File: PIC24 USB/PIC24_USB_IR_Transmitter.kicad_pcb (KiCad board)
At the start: 2 copper layers, 38 parts, among them CON1 USB-MINI-B, P1 CONN_6, P2 CONN_4, P3 CONN_6, P4 CONN_6, P5 CONN_4, P6 CONN_1, P7 CONN_8, P8 CONN_8X2, Q1 2N7002, U1 PIC24FJXXXGB106, U2 LM1117_SOT223_3V3, X1 CRYSTAL_12MHZ

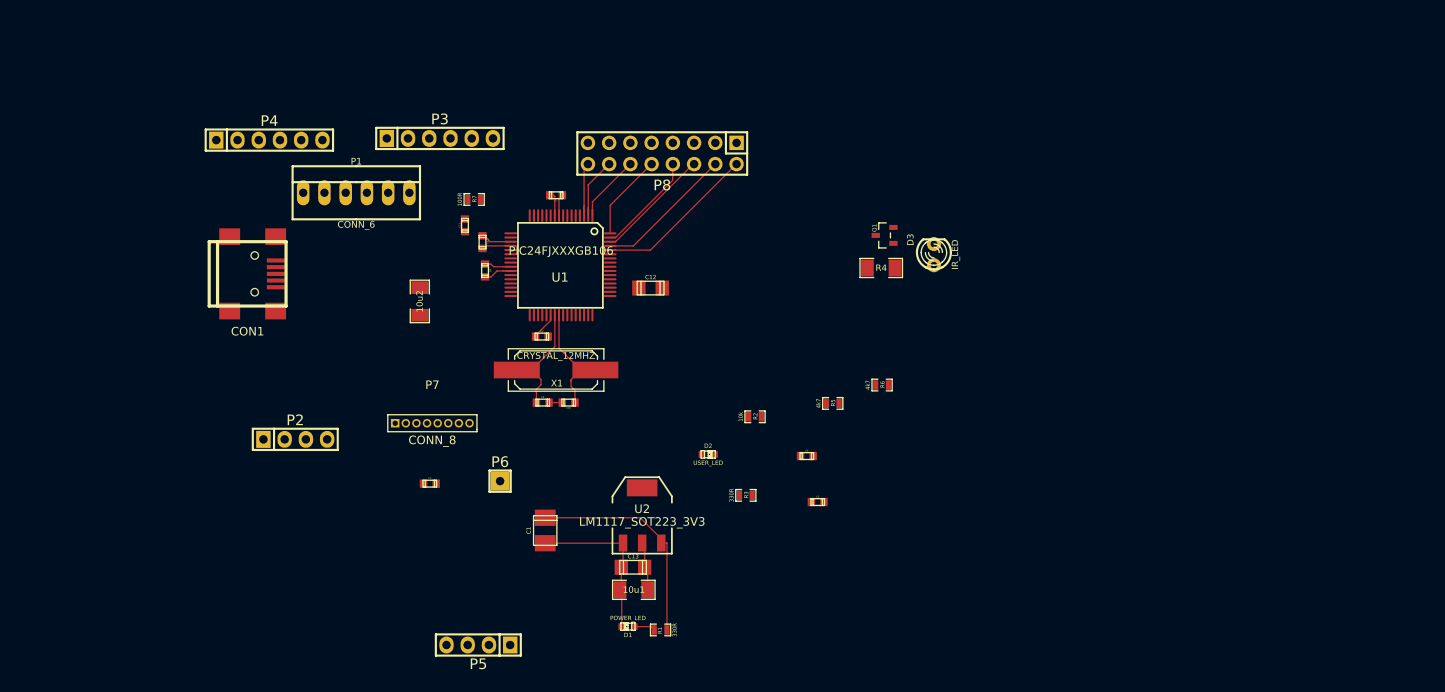
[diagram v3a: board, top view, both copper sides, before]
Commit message: added led display, many additional headers and DAC
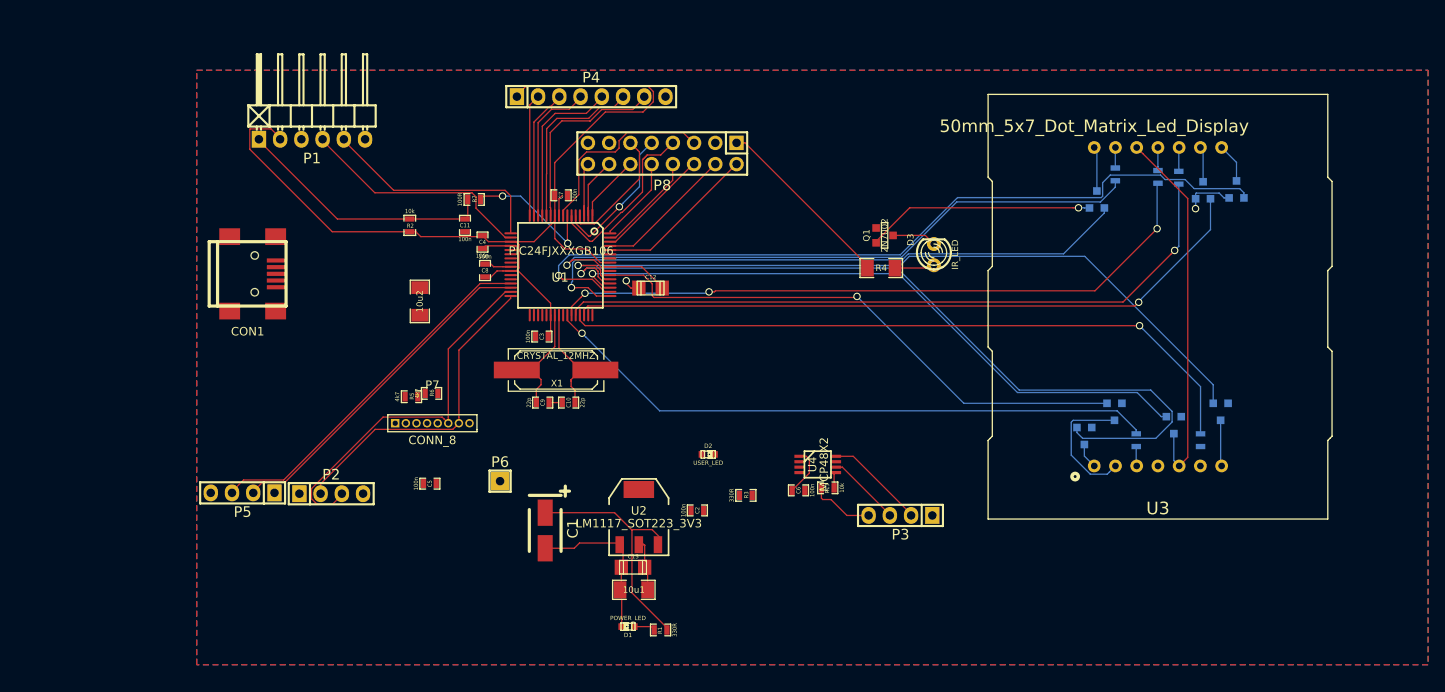
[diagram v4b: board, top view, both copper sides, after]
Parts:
- added Q2: MOSFET_N, SMD_Packages:SOT-23-GDS, B.Cu at (196.6, 55.0)
- added Q3: MOSFET_N, SMD_Packages:SOT-23-GDS, B.Cu at (183.9, 56.1)
- added Q4: MOSFET_N, SMD_Packages:SOT-23-GDS, B.Cu at (200.6, 54.9)
- added Q5: MOSFET_N, SMD_Packages:SOT-23-GDS, B.Cu at (193.1, 83.1)
- added Q6: MOSFET_N, SMD_Packages:SOT-23-GDS, B.Cu at (182.4, 84.4)
- added Q7: MOSFET_N, SMD_Packages:SOT-23-GDS, B.Cu at (198.7, 81.5)
- added Q8: MOSFET_N, SMD_Packages:SOT-23-GDS, B.Cu at (186.0, 81.5)
- added R10: 330R, SMD_Packages:SMD-0603_r, B.Cu at (191.2, 53.4)
- added R11: 330R, SMD_Packages:SMD-0603_r, B.Cu at (193.7, 53.5)
- added R12: 330R, SMD_Packages:SMD-0603_r, B.Cu at (196.3, 84.9)
- added R13: 10k, SMD_Packages:SMD-0603_r, F.Cu at (151.7, 90.6)
- added R8: 330R, SMD_Packages:SMD-0603_r, B.Cu at (186.1, 53.1)
- added R9: 330R, SMD_Packages:SMD-0603_r, B.Cu at (188.6, 84.9)
- added U3: 50mm_5x7_Dot_Matrix_Led_Display, display_hele:50mm5x7DotMatrixLed, F.Cu at (191.2, 70.2)
- added U4: MCP48X2, SMD_Packages:MSOP-8, F.Cu at (150.5, 87.8)
- C1: footprint c_tant_B -> Capacitors_Tantalum_SMD:TantalC_SizeB_EIA-3528_HandSoldering
- C10, C11, C2, C3, C4, C5, C6, C7, C8, C9: footprint Capacitors_SMD:c_0603 -> SMD_Packages:SMD-0603_c
- P1: footprint Connect:PINHEAD1-6 -> Pin_Headers:Pin_Header_Angled_1x06
- P3: value CONN_6 -> CONN_4; footprint Pin_Headers:Pin_Header_Straight_1x06 -> Pin_Headers:Pin_Header_Straight_1x04
- P4: value CONN_6 -> CONN_8; footprint Pin_Headers:Pin_Header_Straight_1x06 -> Pin_Headers:Pin_Header_Straight_1x08
- Q1: footprint Transistors_SMD:sot23 -> SMD_Packages:SOT-23-GDS
- R1, R2, R3, R5, R6, R7: footprint SMD_Packages:SM0603_Resistor -> SMD_Packages:SMD-0603_r
- R4: footprint SMD_Packages:SM1206 -> SMD_Packages:SMD-1206
- moved P3 71.2 mm to (160.4, 93.9), turned to 180 degrees
- moved R6 53.9 mm to (104.3, 79.3)
- moved R5 50.4 mm to (101.9, 79.7)
- moved R2 47.2 mm to (101.7, 59.2), turned to 270 degrees
- moved P4 38.8 mm to (123.4, 43.8)
- moved P5 33.6 mm to (81.7, 91.2)
- moved C2 14.4 mm to (136.1, 93.3)
- moved P1 8.31 mm to (90.0, 48.9)
- moved P2 7.79 mm to (92.3, 91.3)
- moved C6 4.22 mm to (148.2, 90.9), turned to 180 degrees
- moved C7 0.60 mm to (119.8, 55.6)
- moved U2 0.45 mm to (129.1, 94.1)
- turned C1 to 270 degrees
- turned C4 to 90 degrees
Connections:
- C2 pad 1: GND -> +5V
- C2 pad 2: +5V -> GND
- D2 pad 2: GND -> Net-(D2-Pad2)
- P3 pad 1: GND -> +5V
- P3 pad 2: P1D -> /VOUTA
- P3 pad 3: P1C -> /VOUTB
- P3 pad 4: P1B -> GND
- P4 pad 1: GND -> +3.3V
- P4 pad 2: /AN3 -> /MCUSection/AN0
- P4 pad 3: /AN2 -> /MCUSection/AN1
- P4 pad 4: /AN1 -> /MCUSection/AN2
- P4 pad 5: /AN0 -> /MCUSection/AN3
- P4 pad 6: +5V -> /MCUSection/AN4
- P5 pad 1: +5V -> +3.3V
- P5 pad 2: /RX -> /MCUSection/RP29
- P5 pad 3: /TX -> /MCUSection/RP14
- P8 pad 1: Net-(P8-Pad1) -> +5V
- P8 pad 11: Net-(P8-Pad11) -> /MCUSection/RP21/RG6
- P8 pad 13: Net-(P8-Pad13) -> GND
- P8 pad 15: Net-(P8-Pad15) -> GND
- P8 pad 3: Net-(P8-Pad3) -> +3.3V
- P8 pad 5: Net-(P8-Pad5) -> /MCUSection/RP27/RG9
- P8 pad 7: Net-(P8-Pad7) -> /MCUSection/RP19/RG8
- P8 pad 9: Net-(P8-Pad9) -> /MCUSection/RP26/RG7
- U1 pad 11: Net-(U1-Pad11) -> /MCUSection/AN5
- U1 pad 12: Net-(U1-Pad12) -> /MCUSection/AN4
- U1 pad 13: Net-(U1-Pad13) -> /MCUSection/AN3
- U1 pad 14: Net-(U1-Pad14) -> /MCUSection/AN2
- U1 pad 15: Net-(U1-Pad15) -> /MCUSection/AN1
- U1 pad 16: Net-(U1-Pad16) -> /MCUSection/AN0
- U1 pad 29: Net-(U1-Pad29) -> /MCUSection/RP14
- U1 pad 30: Net-(U1-Pad30) -> /MCUSection/RP29
- U1 pad 31: Net-(U1-Pad31) -> SDA
- U1 pad 32: Net-(U1-Pad32) -> SCL
- U1 pad 4: Net-(U1-Pad4) -> /MCUSection/RP21/RG6
- U1 pad 42: Net-(U1-Pad42) -> /Dot Matrix Sheet/C2
- U1 pad 43: SDA -> /Dot Matrix Sheet/C3
- U1 pad 44: SCL -> /Dot Matrix Sheet/C4
- U1 pad 45: Net-(U1-Pad45) -> /Dot Matrix Sheet/C5
- U1 pad 46: Net-(U1-Pad46) -> /MCUSection/PORTD0
- U1 pad 49: Net-(U1-Pad49) -> /MCUSection/PORTD1
- U1 pad 5: Net-(U1-Pad5) -> /MCUSection/RP26/RG7
- U1 pad 50: Net-(U1-Pad50) -> /MCUSection/PORTD2
- U1 pad 51: Net-(U1-Pad51) -> /MCUSection/PORTD3
- U1 pad 52: Net-(U1-Pad52) -> /MCUSection/PORTD4
- U1 pad 53: Net-(U1-Pad53) -> /MCUSection/PORTD5
- U1 pad 54: Net-(U1-Pad54) -> /MCUSection/PORTD6
- U1 pad 55: Net-(U1-Pad55) -> /Dot Matrix Sheet/C1
- U1 pad 6: Net-(U1-Pad6) -> /MCUSection/RP19/RG8
- U1 pad 8: Net-(U1-Pad8) -> /MCUSection/RP27/RG9
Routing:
- net +3.3V: track 19.3 -> 125.2 mm
- net /MCUSection/PORTD4: track 0.00 -> 97.3 mm, vias 0 -> 1
- net /MCUSection/PORTD2: track 0.00 -> 97.1 mm, vias 0 -> 1
- net /MCUSection/PORTD5: track 0.00 -> 89.9 mm, vias 0 -> 1
- net /Dot Matrix Sheet/C5: track 0.00 -> 83.8 mm, vias 0 -> 1
- net /Dot Matrix Sheet/C4: track 0.00 -> 83.4 mm, vias 0 -> 1
- net /MCUSection/PORTD0: track 0.00 -> 83.3 mm, vias 0 -> 1
- net /Dot Matrix Sheet/C3: track 0.00 -> 80.4 mm, vias 0 -> 3
- net /MCUSection/PORTD3: track 0.00 -> 78.7 mm, vias 0 -> 1
- net /Dot Matrix Sheet/C1: track 0.00 -> 76.2 mm, vias 0 -> 1
- net /MCUSection/PORTD1: track 0.00 -> 74.8 mm, vias 0 -> 1
- net /Dot Matrix Sheet/C2: track 0.00 -> 74.6 mm, vias 0 -> 1
- net /MCUSection/PORTD6: track 0.00 -> 66.7 mm, vias 0 -> 1
- net Net-(Q5-PadD): track 0.00 -> 45.2 mm
- net SDA: track 0.00 -> 45.1 mm
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- added copper zone on B.Cu, net GND
- added copper zone on F.Cu, net GND
